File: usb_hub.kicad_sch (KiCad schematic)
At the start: 89 parts, among them J5 USB-C_WE_632723300011, J6 USB-C_WE_632723300011, U16 AP7366_SOT, U17 TPD4E05U06QDQARQ1, U18 AP22615A_TSOT26, U19 TPD4E05U06QDQARQ1, U20 AP22615A_TSOT26, U21 USB7252C, U22 W25Q80DV_USON, U24 TPD4E05U06QDQARQ1, U25 TPD4E05U06QDQARQ1, U27 TPD4E05U06QDQARQ1, U28 TPD4E05U06QDQARQ1, Y2 Oscillator_25MHz_ESC_2016MV

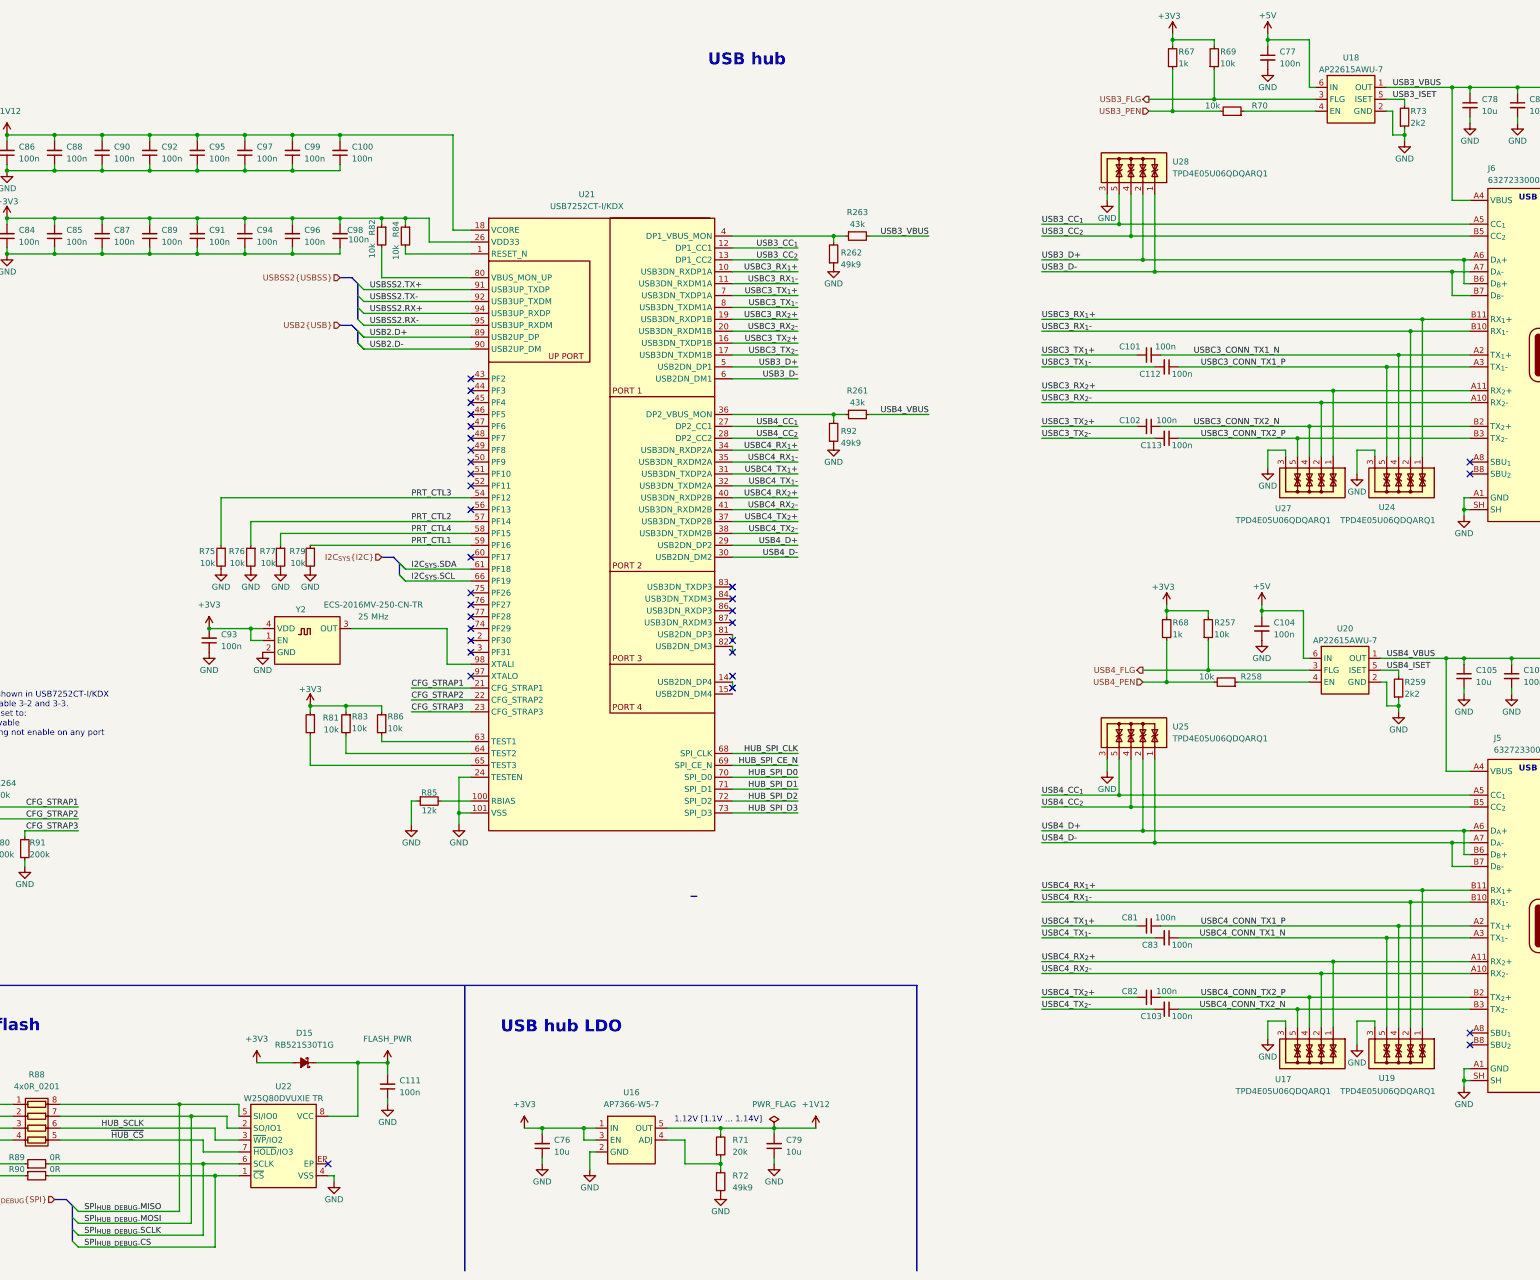
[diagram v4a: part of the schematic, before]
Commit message: [#82837] Finish rerouting USB PD controller, start debug section
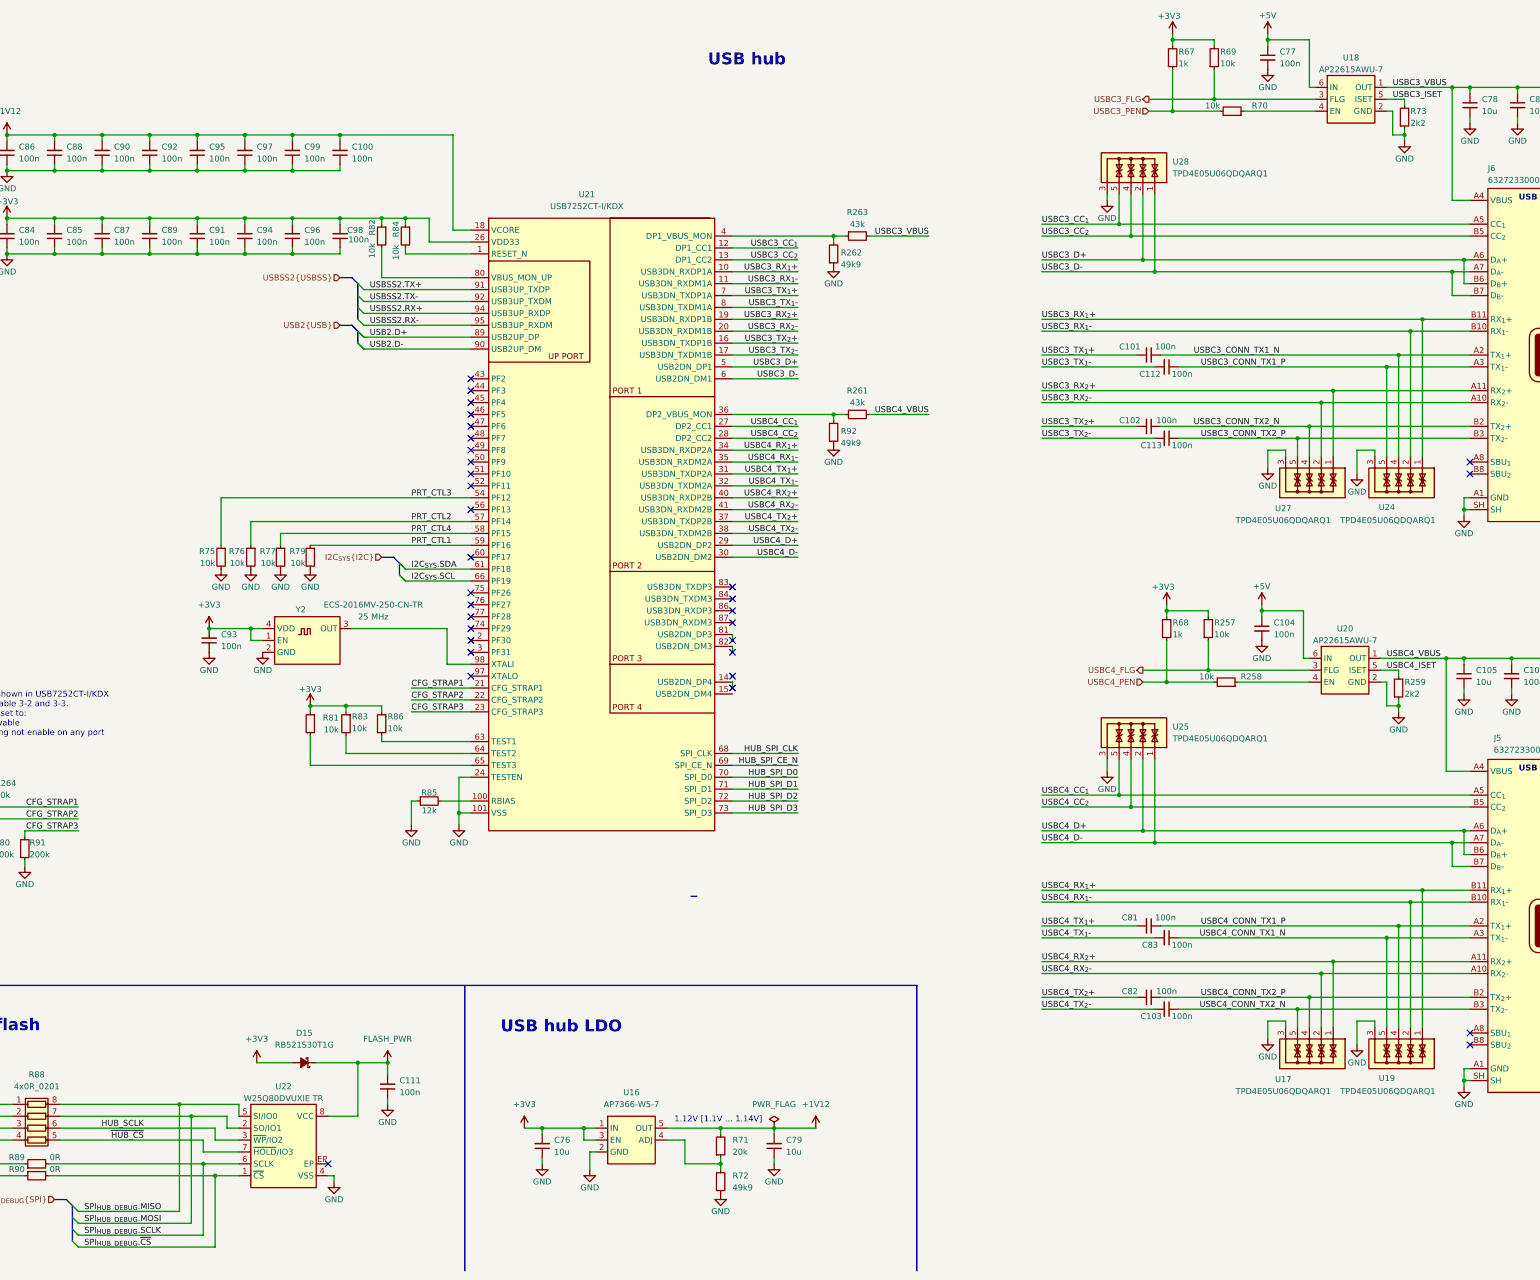
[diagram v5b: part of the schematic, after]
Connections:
- net SPI_{HUB_DEBUG}.CS renamed SPI_{HUB_DEBUG}.~{CS}
- net USB3_CC_{1} renamed USBC3_CC_{1}
- net USB3_CC_{2} renamed USBC3_CC_{2}
- net USB3_D+ renamed USBC3_D+
- net USB3_D- renamed USBC3_D-
- net USB3_FLG renamed USBC3_FLG
- net USB3_ISET renamed USBC3_ISET
- net USB3_PEN renamed USBC3_PEN
- net USB3_VBUS renamed USBC3_VBUS
- net USB4_CC_{1} renamed USBC4_CC_{1}
- net USB4_CC_{2} renamed USBC4_CC_{2}
- net USB4_D+ renamed USBC4_D+
- net USB4_D- renamed USBC4_D-
- net USB4_FLG renamed USBC4_FLG
- net USB4_ISET renamed USBC4_ISET
- net USB4_PEN renamed USBC4_PEN
- net USB4_VBUS renamed USBC4_VBUS
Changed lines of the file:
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@@
 		)
 	)
-	(label "USB4_CC_{2}"
+	(label "USBC4_CC_{2}"
 		(at 260.35 185.42 0)
 		(effects
@@
 		)
 	)
-	(label "USB3_CC_{2}"
+	(label "USBC3_CC_{2}"
 		(at 260.35 63.5 0)
 		(effects
@@
 		)
 	)
-	(label "USB4_VBUS"
+	(label "USBC4_VBUS"
 		(at 236.22 101.6 180)
 		(effects
@@
 		)
 	)
-	(label "USB3_VBUS"
+	(label "USBC3_VBUS"
 		(at 335.28 31.75 0)
 		(effects
@@
 		)
 	)
-	(label "SPI_{HUB_DEBUG}.CS"
+	(label "SPI_{HUB_DEBUG}.~{CS}"
 		(at 55.88 279.4 0)
 		(effects
@@
 		)
 	)
-	(label "USB4_VBUS"
+	(label "USBC4_VBUS"
 		(at 334.01 153.67 0)
 		(effects
@@
 		)
 	)
-	(label "USB4_CC_{2}"
+	(label "USBC4_CC_{2}"
 		(at 208.28 106.68 180)
 		(effects
@@
 		)
 	)
-	(label "USB4_D-"
+	(label "USBC4_D-"
 		(at 260.35 193.04 0)
 		(effects
@@
 		)
 	)
-	(label "USB3_D-"
+	(label "USBC3_D-"
 		(at 208.28 93.98 180)
 		(effects
@@
 		)
 	)
-	(label "USB3_VBUS"
+	(label "USBC3_VBUS"
 		(at 236.22 63.5 180)
 		(effects
@@
 		)
 	)
-	(label "USB3_D-"
+	(label "USBC3_D-"
 		(at 260.35 71.12 0)
 		(effects
@@
 		)
 	)
-	(label "USB3_CC_{2}"
+	(label "USBC3_CC_{2}"
 		(at 208.28 68.58 180)
 		(effects
@@
 		)
 	)
-	(label "USB3_CC_{1}"
+	(label "USBC3_CC_{1}"
 		(at 208.28 66.04 180)
 		(effects
@@
 		)
 	)
-	(label "USB3_ISET"
+	(label "USBC3_ISET"
 		(at 335.28 34.29 0)
 		(effects
@@
 		)
 	)
-	(label "USB4_ISET"
+	(label "USBC4_ISET"
 		(at 334.01 156.21 0)
 		(effects
@@
 		)
 	)
-	(label "USB4_D-"
+	(label "USBC4_D-"
 		(at 208.28 132.08 180)
 		(effects
@@
 		)
 	)
-	(label "USB4_CC_{1}"
+	(label "USBC4_CC_{1}"
 		(at 260.35 182.88 0)
 		(effects
@@
 		)
 	)
-	(label "USB3_D+"
+	(label "USBC3_D+"
 		(at 208.28 91.44 180)
 		(effects
@@
 		)
 	)
-	(label "USB4_D+"
+	(label "USBC4_D+"
 		(at 260.35 190.5 0)
 		(effects
@@
 		)
 	)
-	(label "USB3_D+"
+	(label "USBC3_D+"
 		(at 260.35 68.58 0)
 		(effects
@@
 		)
 	)
-	(label "USB3_CC_{1}"
+	(label "USBC3_CC_{1}"
 		(at 260.35 60.96 0)
 		(effects
@@
 		)
 	)
-	(label "USB4_D+"
+	(label "USBC4_D+"
 		(at 208.28 129.54 180)
 		(effects
@@
 		)
 	)
-	(label "USB4_CC_{1}"
+	(label "USBC4_CC_{1}"
 		(at 208.28 104.14 180)
 		(effects
@@
 		)
 	)
-	(hierarchical_label "USB4_PEN"
+	(hierarchical_label "USBC4_PEN"
 		(shape input)
 		(at 281.94 158.75 180)
@@
 		)
 	)
-	(hierarchical_label "USB4_FLG"
+	(hierarchical_label "USBC4_FLG"
 		(shape output)
 		(at 281.94 156.21 180)
@@
 		)
 	)
-	(hierarchical_label "USB3_PEN"
+	(hierarchical_label "USBC3_PEN"
 		(shape input)
 		(at 283.21 36.83 180)
@@
 		)
 	)
-	(hierarchical_label "USB3_FLG"
+	(hierarchical_label "USBC3_FLG"
 		(shape output)
 		(at 283.21 34.29 180)

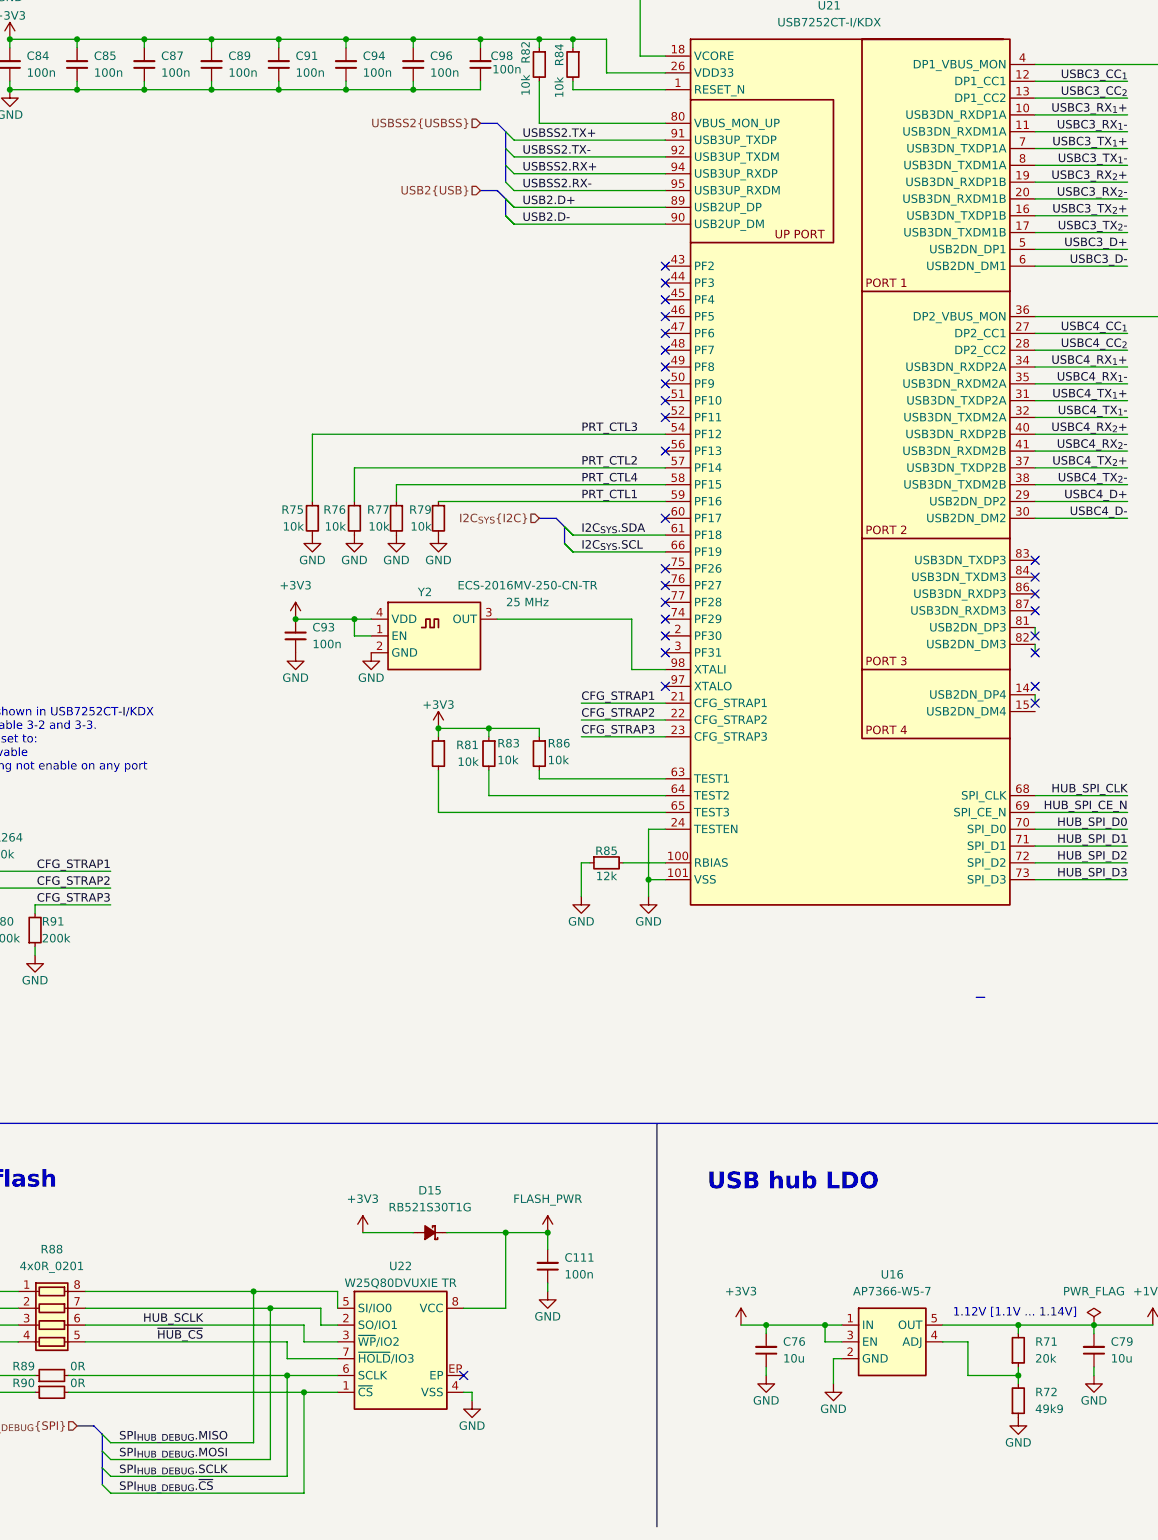
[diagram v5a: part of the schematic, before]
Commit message: [#82837] Finish mapping PCIe and SFP+ connections on SoM
[#82837] WIP: correct ERC errors

[#82837] WIP: correct ERC errors, fix signal direction of most buses

[#82837] Fix all ERC errors
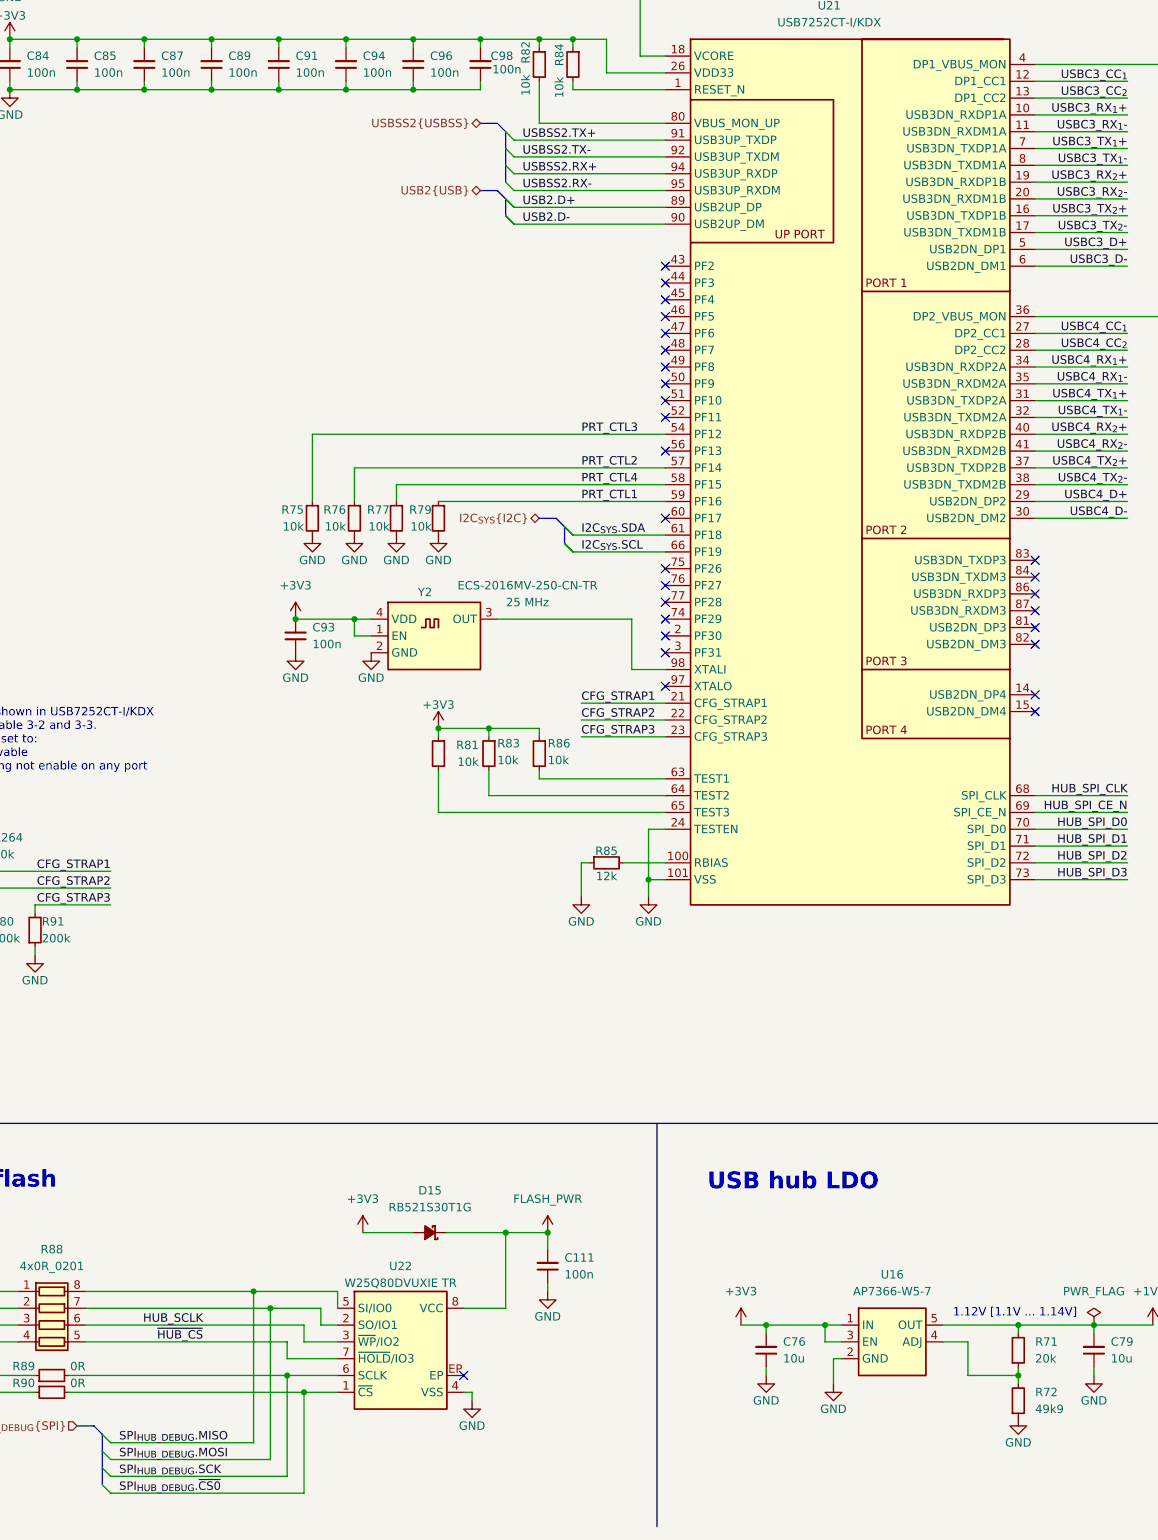
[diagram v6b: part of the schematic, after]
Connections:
- net SPI_{HUB_DEBUG}.SCLK renamed SPI_{HUB_DEBUG}.SCK
- net SPI_{HUB_DEBUG}.~{CS} renamed SPI_{HUB_DEBUG}.~{CS0}
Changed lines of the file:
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@@
 	)
 	(no_connect
-		(at 194.31 152.4)
+		(at 194.31 151.13)
 	)
 	(no_connect
@@
 	)
 	(no_connect
-		(at 194.31 160.02)
+		(at 194.31 161.29)
 	)
 	(no_connect
@@
 	)
 	(no_connect
-		(at 194.31 157.48)
+		(at 194.31 158.75)
 	)
 	(no_connect
@@
 	)
 	(no_connect
-		(at 194.31 149.86)
+		(at 194.31 148.59)
 	)
 	(no_connect
@@
 	(wire
 		(pts
-			(xy 194.31 149.86) (xy 194.31 148.59)
-		)
-		(stroke
-			(width 0)
-			(type default)
-		)
-	)
-	(wire
-		(pts
 			(xy 124.46 67.31) (xy 138.43 67.31)
 		)
@@
 		)
 	)
-	(polyline
-		(pts
-			(xy 186.69 204.47) (xy 185.42 204.47)
-		)
-		(stroke
-			(width 0)
-			(type default)
-		)
-	)
 	(wire
 		(pts
@@
 	(wire
 		(pts
-			(xy 194.31 152.4) (xy 194.31 151.13)
-		)
-		(stroke
-			(width 0)
-			(type default)
-		)
-	)
-	(wire
-		(pts
 			(xy 287.02 158.75) (xy 297.18 158.75)
 		)
@@
 	(wire
 		(pts
-			(xy 194.31 160.02) (xy 194.31 158.75)
-		)
-		(stroke
-			(width 0)
-			(type default)
-		)
-	)
-	(wire
-		(pts
 			(xy 337.82 41.91) (xy 337.82 43.18)
 		)
@@
 		)
 	)
-	(label "SPI_{HUB_DEBUG}.~{CS}"
+	(label "SPI_{HUB_DEBUG}.~{CS0}"
 		(at 55.88 279.4 0)
 		(effects
@@
 		)
 	)
-	(label "SPI_{HUB_DEBUG}.SCLK"
+	(label "SPI_{HUB_DEBUG}.SCK"
 		(at 55.88 276.86 0)
 		(effects
@@
 	)
 	(hierarchical_label "USB2{USB}"
-		(shape input)
+		(shape bidirectional)
 		(at 110.49 82.55 180)
 		(effects
@@
 	)
 	(hierarchical_label "I2C_{SYS}{I2C}"
-		(shape input)
+		(shape bidirectional)
 		(at 119.38 132.08 180)
 		(effects
@@
 	)
 	(hierarchical_label "USBSS2{USBSS}"
-		(shape input)
+		(shape bidirectional)
 		(at 110.49 72.39 180)
 		(effects
